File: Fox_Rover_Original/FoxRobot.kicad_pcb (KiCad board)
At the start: 2 copper layers, 102.9 x 116.8 mm, 38 parts, among them J1 Screw_Terminal_01x02, J2 XT60-M_Green, J3 XT60-M_Red, J4 Screw_Terminal_01x02, J5 Conn_02x10_Odd_Even, J6 Screw_Terminal_01x02, J7 Conn_02x10_Odd_Even, K1 40.52.7.012.0000, K2 G2RK-1_12DC, K3 ADJH23005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

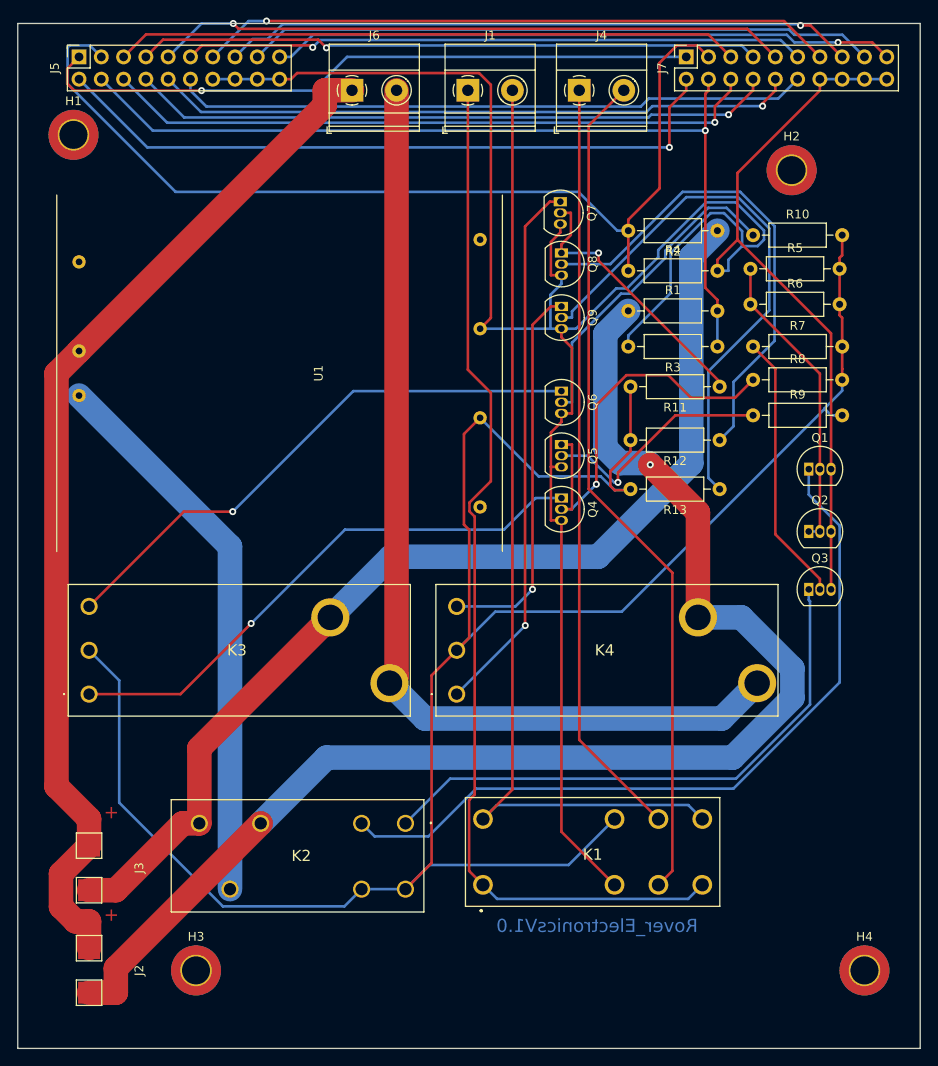
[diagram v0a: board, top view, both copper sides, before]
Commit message: Adjusted libraries pathing
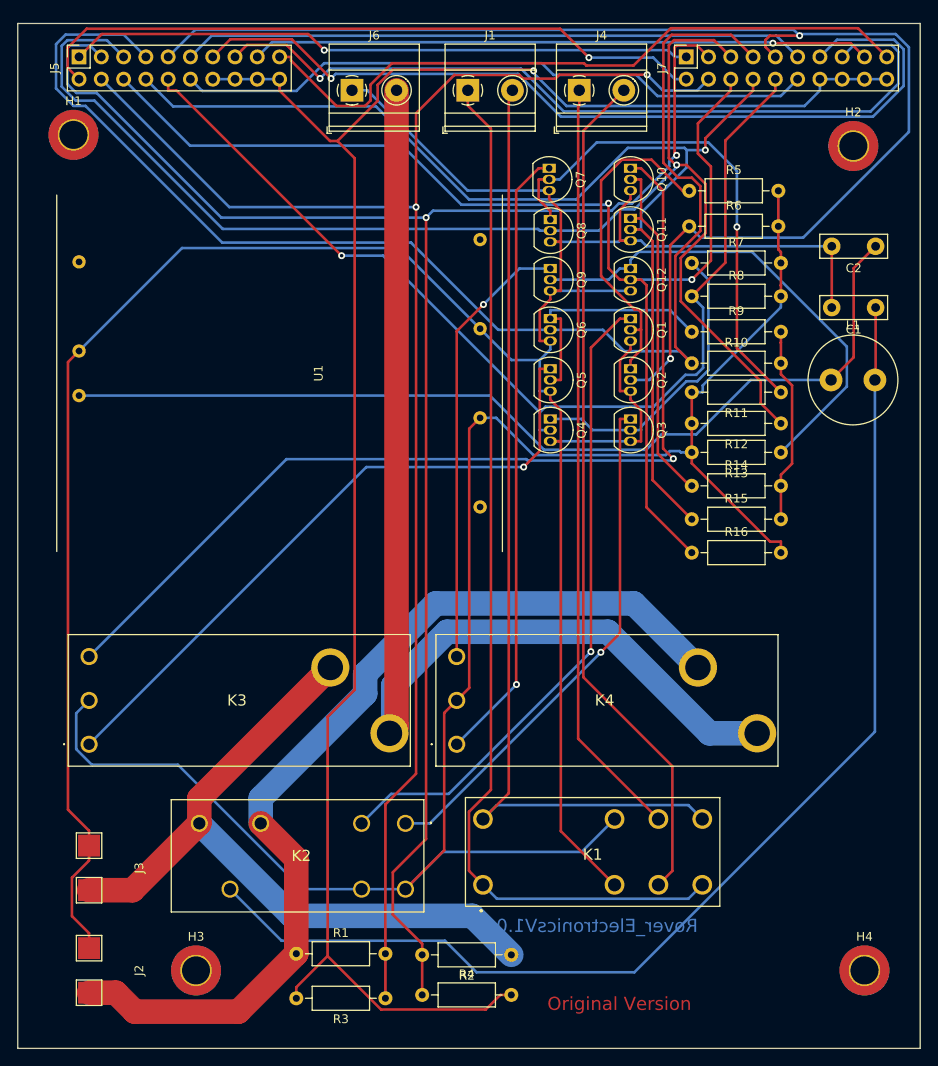
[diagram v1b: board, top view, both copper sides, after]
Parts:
- added C1: 330uF, Capacitor_THT:C_Disc_D7.5mm_W2.5mm_P5.00mm, F.Cu at (110.5, 43.8)
- added C2: 100uF, Capacitor_THT:C_Disc_D7.5mm_W2.5mm_P5.00mm, F.Cu at (110.5, 36.8)
- added L1: L, Inductor_THT:L_Radial_D10.0mm_P5.00mm_Fastron_07M, F.Cu at (105.4, 52.1)
- added Q10: BS170, Package_TO_SOT_THT:TO-92_Inline, F.Cu at (82.5, 27.9)
- added Q11: BS170, Package_TO_SOT_THT:TO-92_Inline, F.Cu at (82.5, 33.7)
- added Q12: BS170, Package_TO_SOT_THT:TO-92_Inline, F.Cu at (82.5, 39.4)
- added R14: 10k, Resistor_THT:R_Axial_DIN0207_L6.3mm_D2.5mm_P10.16mm_Horizontal, F.Cu at (89.5, 64.1)
- added R15: 10k, Resistor_THT:R_Axial_DIN0207_L6.3mm_D2.5mm_P10.16mm_Horizontal, F.Cu at (89.5, 67.9)
- added R16: 10k, Resistor_THT:R_Axial_DIN0207_L6.3mm_D2.5mm_P10.16mm_Horizontal, F.Cu at (89.5, 71.8)
- J5: value Conn_02x10_Odd_Even -> hExt_in
- J7: value Conn_02x10_Odd_Even -> Pin_Header
- K2: value G2RK-1_12DC -> BATTERY_LOGIC_RELAY
- K3: value ADJH23005 -> POWER_RELAY_RED
- K4: value ADJH23005 -> POWER_RELAY_GREEN
- R10, R11, R12, R13, R5, R6, R7, R8, R9: value R -> 10k
- moved R2 85.8 mm to (69.0, 117.6)
- moved R4 85.8 mm to (58.8, 122.2)
- moved R3 83.4 mm to (54.6, 122.6)
- moved R1 82.5 mm to (44.5, 117.5)
- moved Q3 28.1 mm to (82.5, 56.5), turned to 270 degrees
- moved Q2 27.5 mm to (82.5, 50.8), turned to 270 degrees
- moved Q1 26.6 mm to (82.5, 45.1), turned to 270 degrees
- moved R10 16.2 mm to (89.5, 50.2)
- moved R7 11.8 mm to (89.5, 38.7)
- moved R8 11.8 mm to (89.5, 42.5)
- moved R9 11.8 mm to (89.5, 46.6)
- moved R5 11.3 mm to (89.2, 30.5)
- moved R6 11.3 mm to (89.2, 34.6)
- moved Q4 9.11 mm to (73.4, 56.5)
- moved Q5 8.73 mm to (73.4, 50.8)
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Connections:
- J2 pad 1: Net-(J2-Pad1) -> Net-(C1-Pad2)
- J3 pad 1: Net-(J2-Pad1) -> Net-(C1-Pad2)
- J6 pad 1: Net-(J2-Pad1) -> Net-(C1-Pad2)
- K1 pad 12: GND -> Net-(C1-Pad2)
- K2 pad 5: Net-(K2-Pad5) -> Net-(C1-Pad1)
- Q1 pad 3: GND -> Net-(C1-Pad2)
- Q2 pad 2: Net-(Q1-Pad2) -> /A9
- Q2 pad 3: GND -> Net-(C1-Pad2)
- Q3 pad 3: GND -> Net-(C1-Pad2)
- Q4 pad 1: Net-(K3-Pad1) -> Net-(Q3-Pad2)
- Q4 pad 2: Net-(Q4-Pad2) -> /A10
- Q4 pad 3: GND -> Net-(C1-Pad2)
- Q5 pad 1: Net-(Q4-Pad2) -> Net-(K3-Pad1)
- Q5 pad 3: GND -> Net-(C1-Pad2)
- Q6 pad 1: Net-(K3-Pad2) -> Net-(Q5-Pad2)
- Q6 pad 2: Net-(Q6-Pad2) -> /A7
- Q6 pad 3: GND -> Net-(C1-Pad2)
- Q7 pad 3: GND -> Net-(C1-Pad2)
- Q8 pad 2: Net-(Q8-Pad2) -> /A5
- Q8 pad 3: GND -> Net-(C1-Pad2)
- Q9 pad 3: GND -> Net-(C1-Pad2)
- R10 pad 1: Net-(Q6-Pad2) -> /A7
- R10 pad 2: +5V -> Net-(R10-Pad2)
- R12 pad 1: Net-(Q8-Pad2) -> /A5
- R6 pad 1: Net-(Q1-Pad2) -> /A9
- R8 pad 1: Net-(Q4-Pad2) -> /A10
- R9 pad 2: +5V -> Net-(R10-Pad2)
- U1 pad 3: Net-(J2-Pad1) -> Net-(C1-Pad2)
- U1 pad 4: Net-(K2-Pad5) -> +24V
- U1 pad 6: GND -> Net-(C1-Pad2)
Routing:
- net Net-(C1-Pad2): track 0.00 -> 330.7 mm
- net Net-(C1-Pad1): track 0.00 -> 137.2 mm
- net Net-(J2-Pad1): track 118.6 -> 0.00 mm
- net +24V: track 0.00 -> 108.9 mm
- net /A3: track 111.6 -> 196.1 mm, vias 0 -> 2
- net /A7: track 71.1 -> 155.0 mm, vias 1 -> 0
- net GND: track 298.0 -> 214.3 mm, vias 0 -> 1
- net /A9: track 72.4 -> 155.0 mm, vias 1 -> 2
- net /A5: track 71.3 -> 152.5 mm, vias 0 -> 1
- net /A4: track 102.5 -> 181.0 mm, vias 1 -> 2
- net /A6: track 75.1 -> 139.4 mm, vias 1 -> 2
- net Net-(K2-Pad5): track 63.4 -> 0.00 mm
- net /A8: track 73.6 -> 131.4 mm
- net Net-(Q8-Pad2): track 56.3 -> 0.00 mm
- net Net-(K3-Pad2): track 64.0 -> 111.9 mm
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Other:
- board text added: "Original Version"
